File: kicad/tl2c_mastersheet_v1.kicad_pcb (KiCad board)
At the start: 4 copper layers, 117.5 x 66 mm, 88 parts, among them IC101 ATTINY20-X, P101 12VDC, P102 I2C Master, P103 Spare, P104 ISP Header, P105 LED_DRIVER, P106 240VAC, P107 LED_DRIVER, P108 LED_OUT, P301 PIR13, Q301 IRLML2502, Q302 IRLML2502, Q303 IRLML2502, Q401 IRLML2502, Q402 IRLML2502, Q403 IRLML2502, SW101 TL3315NF160Q, U201 LF120ABDT-TR, U202 TPS70933

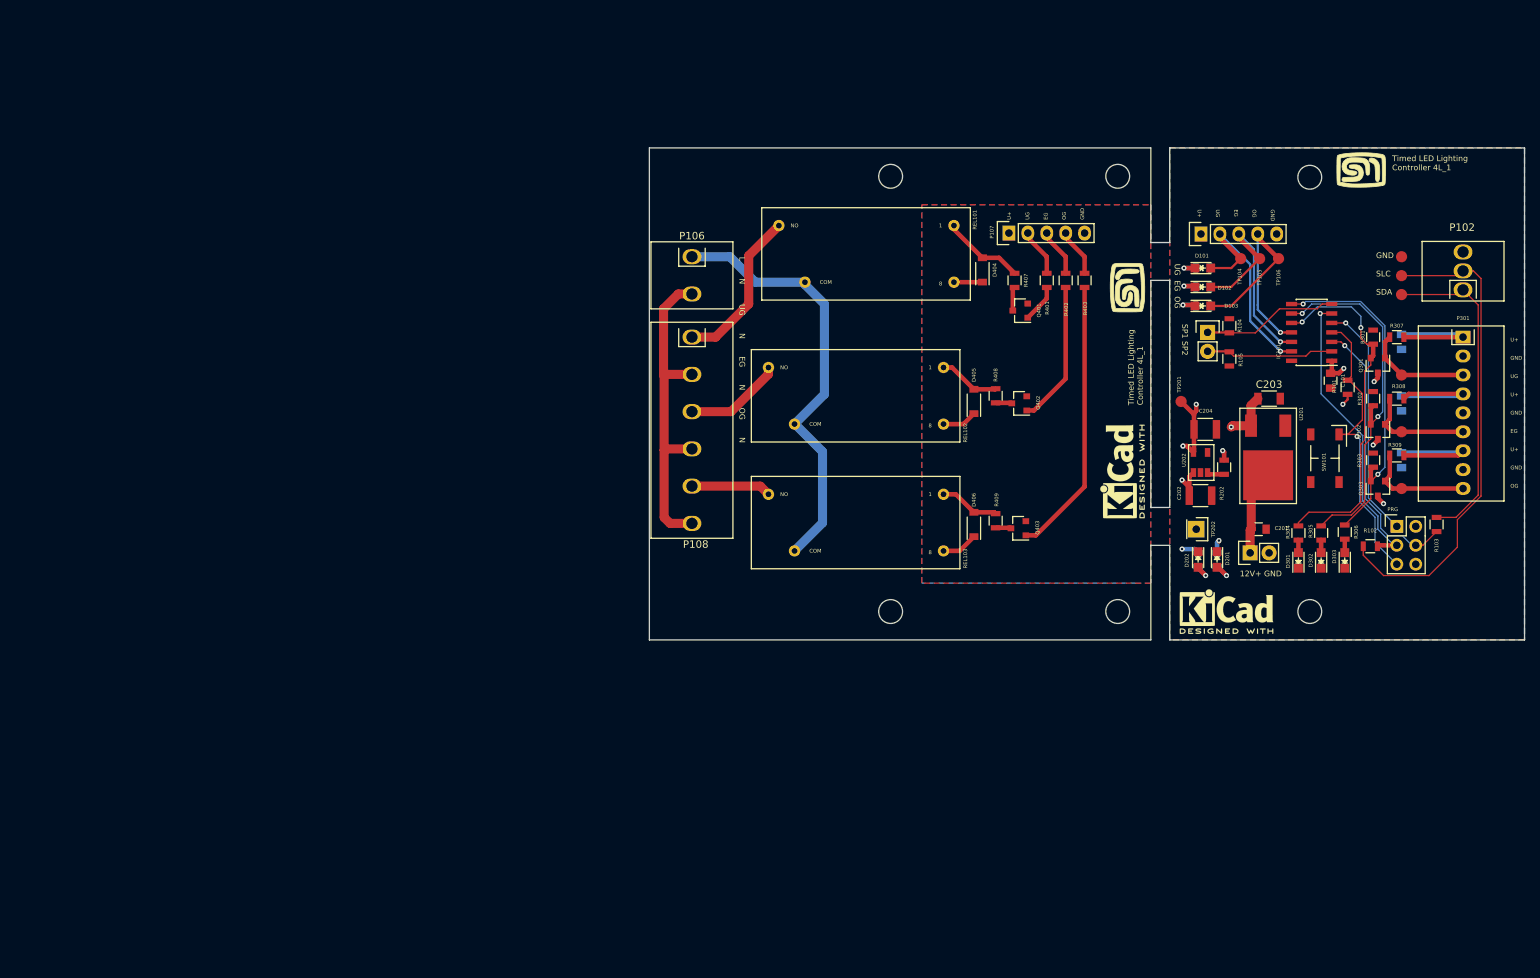
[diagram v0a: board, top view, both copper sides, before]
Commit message: Created the Gerbers and submitted the order for boards and stensils
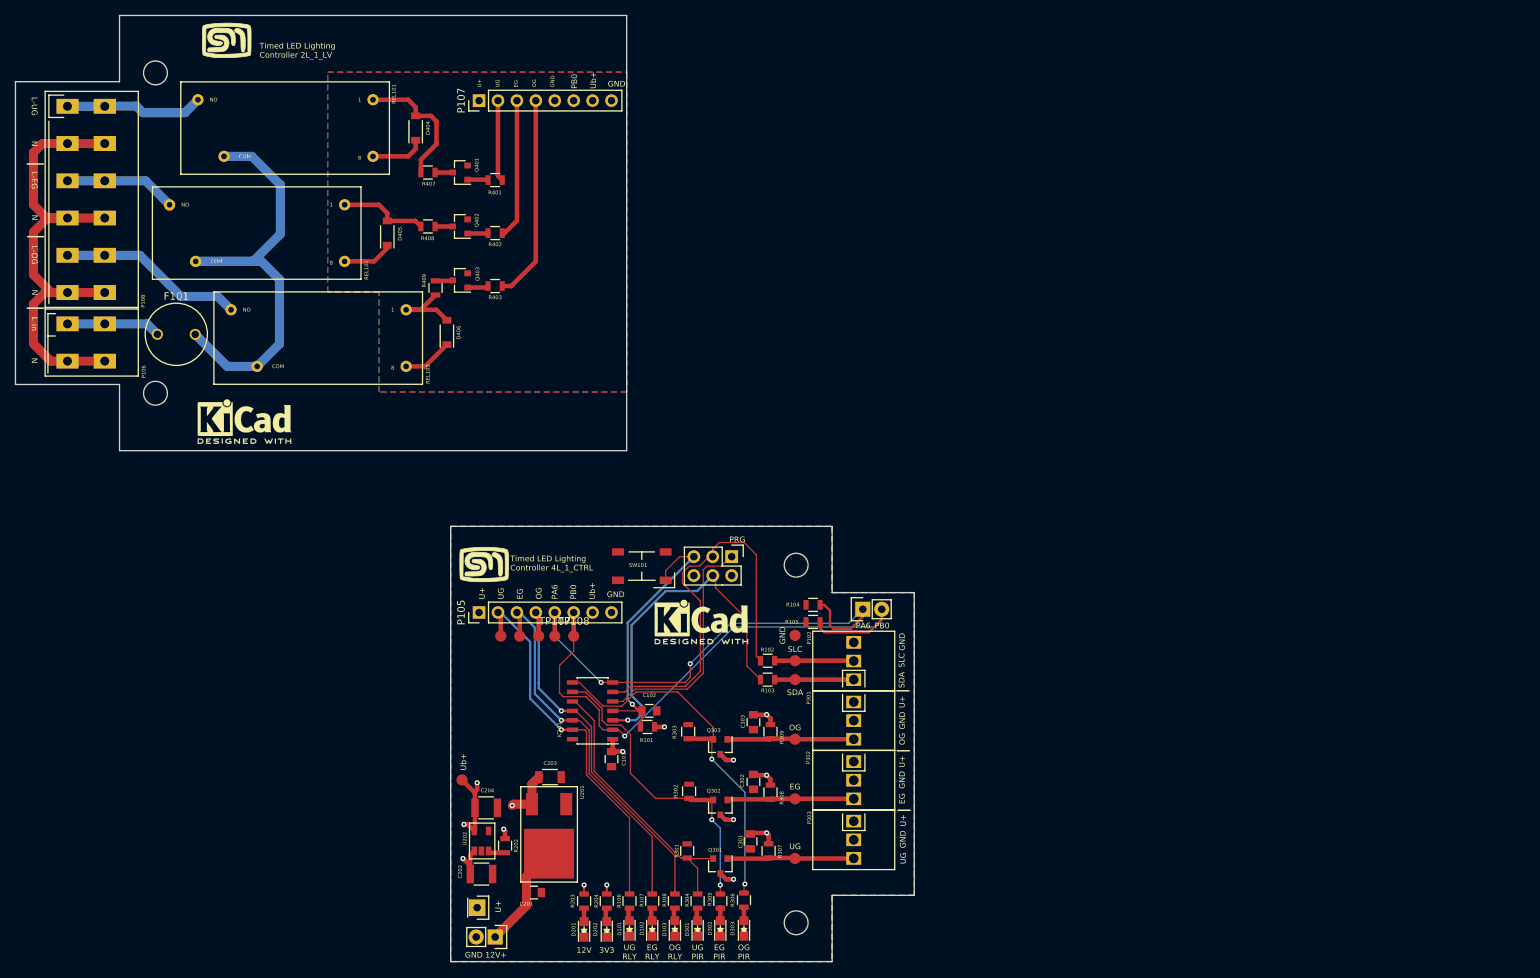
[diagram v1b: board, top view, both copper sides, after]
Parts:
- removed the REF** at (182.2, 132.1)
- removed the REF** at (182.2, 73.7)
- added C102: 100n 50V, Capacitors_SMD:C_0805, F.Cu at (119.4, 145.4)
- added F101: 500mA, tl2c-footprint:Fuse_TE5_Littlefuse-ESKA_887_O14, F.Cu at (55.9, 94.9)
- added P302: CONN_PIR_EG, tl2c-footprint:Spring_Terminal_Block_1_x_3, F.Cu at (146.8, 152.2)
- added P303: CONN_PIR_UG, tl2c-footprint:Spring_Terminal_Block_1_x_3, F.Cu at (146.8, 160.2)
- added TP107: PA6, Measurement_Points:Measurement_Point_Round-SMD-Pad_Small, F.Cu at (106.7, 135.4)
- added TP108: PB0, Measurement_Points:Measurement_Point_Round-SMD-Pad_Small, F.Cu at (109.2, 135.4)
- C101: value 100n 10V -> 100n 50V
- C301, C302, C303, R106, R107, R108, R203, R204: moved to F.Cu
- P105, P107: footprint Pin_Headers:Pin_Header_Straight_1x05 -> Pin_Headers:Pin_Header_Straight_1x08_Pitch2.54mm
- P106: footprint tl2c-footprint:Spring_Terminal_Block_1_x_2_5mm -> tl2c-footprint:TERMINAL_BLOCK_2_5MM_5MM
- P108: footprint tl2c-footprint:Spring_Terminal_Block_1_x_6_5mm -> tl2c-footprint:TERMINAL_BLOCK_6_5MM_5MM
- P301: value PIR13 -> CONN_PIR_OG; footprint tl2c-footprint:Spring_Terminal_Block_1_x_9 -> tl2c-footprint:Spring_Terminal_Block_1_x_3
- moved G*** 129.1 mm to (97.2, 125.7)
- moved G*** 125.4 mm to (62.6, 55.4), turned to 0 degrees
- moved REF*** 118.0 mm to (65.0, 106.6), turned to 0 degrees
- moved D101 117.4 mm to (116.7, 174.6), turned to 90 degrees
- moved R301 115.0 mm to (124.5, 164.2)
- moved R106 114.6 mm to (116.7, 170.9), turned to 270 degrees
- moved P101 113.7 mm to (98.7, 175.8), turned to 270 degrees
- moved D102 113.5 mm to (119.8, 174.6), turned to 90 degrees
- moved TP106 111.5 mm to (104.5, 135.4)
- moved TP104 111.5 mm to (99.4, 135.4)
- moved TP105 111.5 mm to (102.0, 135.4)
- moved Q301 110.9 mm to (128.9, 166.2)
- moved R107 110.7 mm to (119.8, 170.9), turned to 270 degrees
- moved C301 110.1 mm to (133.0, 162.9)
- moved D103 109.6 mm to (122.8, 174.6), turned to 90 degrees
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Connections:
- net /Reset renamed /~Reset
- D101 pad 1: Net-(D101-Pad1) -> GND
- D101 pad 2: /RelayUG -> Net-(D101-Pad2)
- D102 pad 1: Net-(D102-Pad1) -> GND
- D102 pad 2: /RelayEG -> Net-(D102-Pad2)
- D103 pad 1: Net-(D103-Pad1) -> GND
- D103 pad 2: /RelayOG -> Net-(D103-Pad2)
- IC101 pad 2: /Spare2 -> /GPIO_PB0
- IC101 pad 7: /Spare1 -> /GPIO_PA6
- P103 pad 1: /Spare1 -> /GPIO_PA6
- P103 pad 2: /Spare2 -> /GPIO_PB0
- P105 pad 5: GND -> /GPIO_PA6
- P107 pad 5: GNDA -> Net-(P107-Pad5)
- P301 pad 3: /PIR13/PIR_UG -> /PIR13/PIR_OG
- R104 pad 2: /Spare1 -> /GPIO_PA6
- R105 pad 2: /Spare2 -> /GPIO_PB0
- R106 pad 1: Net-(D101-Pad1) -> /RelayUG
- R106 pad 2: GND -> Net-(D101-Pad2)
- R107 pad 1: Net-(D102-Pad1) -> /RelayEG
- R107 pad 2: GND -> Net-(D102-Pad2)
- R108 pad 1: Net-(D103-Pad1) -> /RelayOG
- R108 pad 2: GND -> Net-(D103-Pad2)
- REL101 pad 6: /Lin -> Net-(F101-Pad2)
- REL102 pad 6: /Lin -> Net-(F101-Pad2)
- REL103 pad 6: /Lin -> Net-(F101-Pad2)
- SW101 pad 2: (no net) -> Net-(SW101-Pad2)
- SW101 pad 4: (no net) -> Net-(SW101-Pad4)
- U202 pad 4: (no net) -> Net-(U202-Pad4)
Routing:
- net /GPIO_PB0: track 0.00 -> 79.2 mm, vias 0 -> 1
- net /GPIO_PA6: track 0.00 -> 66.4 mm, vias 0 -> 2
- net Net-(F101-Pad2): track 0.00 -> 64.0 mm
- net /SCL: track 66.0 -> 10.6 mm
- net /Lin: track 58.4 -> 12.6 mm
- net /PIR13/U+: track 65.7 -> 26.1 mm, vias 4 -> 7
- net Net-(Q403-Pad1): track 37.3 -> 2.83 mm
- net /SDA: track 43.7 -> 10.6 mm
- net /Neutral: track 44.4 -> 70.1 mm
- net /LED Driver/Relay_OG: track 6.45 -> 27.5 mm
- net /RelayUG: track 29.6 -> 50.5 mm
- net /RelayEG: track 30.9 -> 50.2 mm
- net /Spare1: track 18.6 -> 0.00 mm
- net /RelayOG: track 32.2 -> 50.2 mm
- net /Spare2: track 17.2 -> 0.00 mm
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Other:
- board size 117.5 x 66 mm -> 120.7 x 127 mm
- board text added: "12V"
- board text added: "3V3"
- board text added: "EG"
- board text added: "EG PIR"
- board text added: "EG RLY"
- board text added: "GND"
- board text added: "GND 12V+"
- board text added: "L-EG"
- board text added: "L-OG"
- board text added: "L-UG"
- board text added: "L-in"
- board text added: "N"
- board text added: "OG"
- board text added: "OG PIR"
- board text added: "OG RLY"
- board text added: "PA6"
- board text added: "PB0"
- board text added: "SDA"
- board text added: "SLC"
- board text added: "Timed LED Lighting Controller 2L_1_LV"
- board text added: "Timed LED Lighting Controller 4L_1_CTRL"
- board text added: "U+"
- board text added: "UG"
- board text added: "UG PIR"
- board text added: "UG RLY"
- board text added: "Ub+"
- board text removed: "12V+ GND"
- board text removed: "CUT OUT"
- board text removed: "GND OG EG UG U+"
- board text removed: "GND SLC SDA"
- board text removed: "L N UG N EG N OG N"
- board text removed: "SP1 SP2"
- board text removed: "Timed LED Lighting Controller 4L_1"
- board text removed: "U+ GND UG U+ GND EG U+ GND OG"
- board text removed: "UG EG OG"
